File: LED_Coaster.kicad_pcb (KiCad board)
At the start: 2 copper layers, 100 x 100 mm, 48 parts, among them IC1 ESP32-WROOM-32E-N4, IC2 VCNL4010-GS08, J1 JST_2P_1769, J3 micro_usb_female_105164-0001, Q1 DMG3415U, Q2 MBT2222ADW1T1, U1 AP2112-3.3, U2 CP2104, U3 MCP73831-2-OT

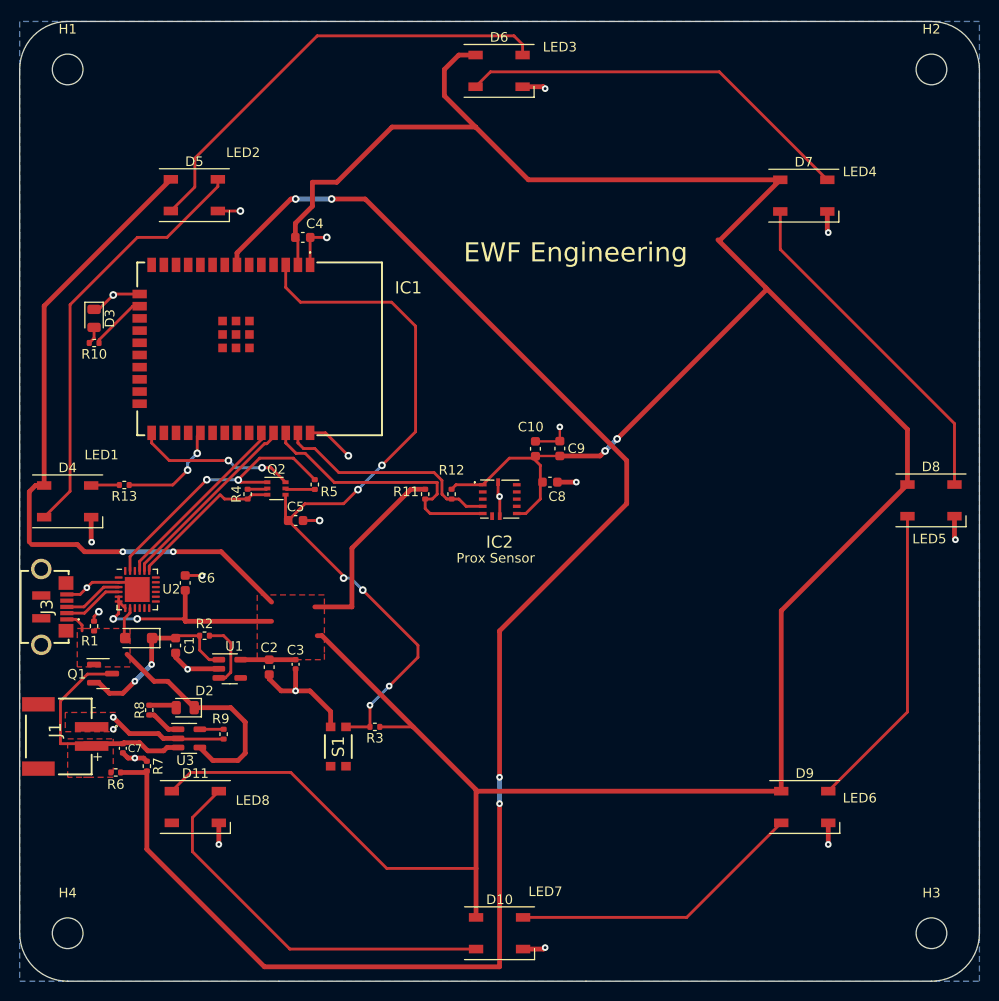
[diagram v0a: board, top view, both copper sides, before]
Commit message: Rerouted some traces, changed diode to a standard 0.7/0.8V drop, tried to improve power routing. Fixed "-VBATT" to "+VBATT"
My work is a bit messy still, but it should be fine like this. Still haven't done the math on the LDO, need to figure out what the power of the system is.
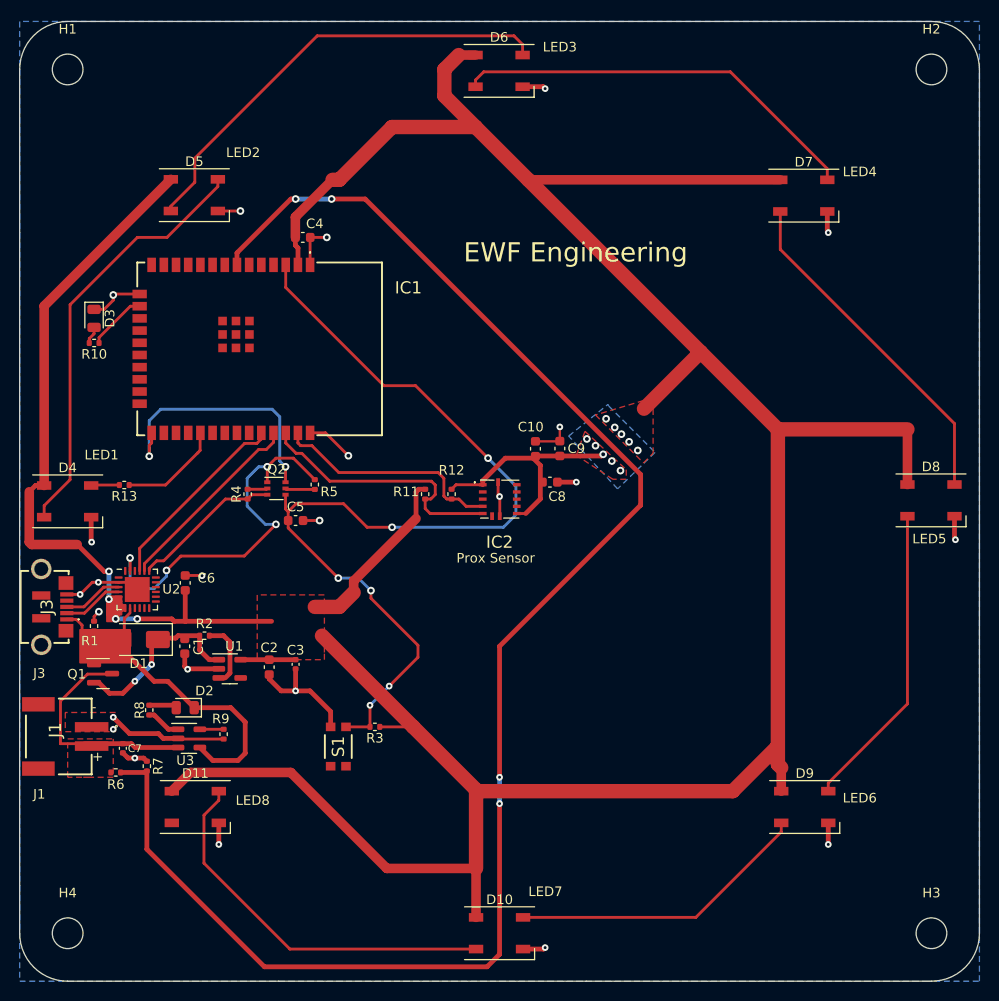
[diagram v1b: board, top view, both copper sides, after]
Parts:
- D1: value MBR1020VL -> MRA4003T3G; footprint Diode_SMD:D_SOD-123F -> Diode_SMD:D_SMA
- moved C1 0.95 mm to (42.2, 90.1)
- moved D1 0.15 mm to (37.4, 89.4)
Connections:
- net -BATT renamed /VBATT
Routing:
- net /RESET: track 80.6 -> 99.2 mm
- net +3.3V: track 433.2 -> 416.6 mm, vias 6 -> 14
- net /GPIO0: track 16.7 -> 27.7 mm
- net /DTR: track 29.1 -> 39.6 mm, vias 2 -> 4
- net Net-(D6-DOUT): track 42.0 -> 43.0 mm
- net Net-(D10-DOUT): track 41.2 -> 40.2 mm
- net /RXD0: track 19.6 -> 20.4 mm
- net Net-(D10-DIN): track 31.0 -> 31.5 mm
- net /RTS: track 16.3 -> 15.7 mm
- net /SCL: track 28.4 -> 27.9 mm
- net /GPIO5: track 11.2 -> 10.9 mm, vias 2 -> 0
- net GND: track 89.4 -> 89.2 mm, vias 23 -> 24
- added copper zone on B.Cu, net +3.3V
- removed copper zone on F.Cu, net VBUS
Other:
- board text added: "J1"
- board text added: "J3"
